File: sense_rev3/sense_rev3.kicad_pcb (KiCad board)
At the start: 2 copper layers, 68 x 52 mm, 46 parts, among them J1 Audio-Jack-4, P1 CONN_02X05, Q1 TSM2301, SW1 SW_SPST, U1 TLV8802, U2 MDBT42Q, U3 PIR, Y1 Crystal

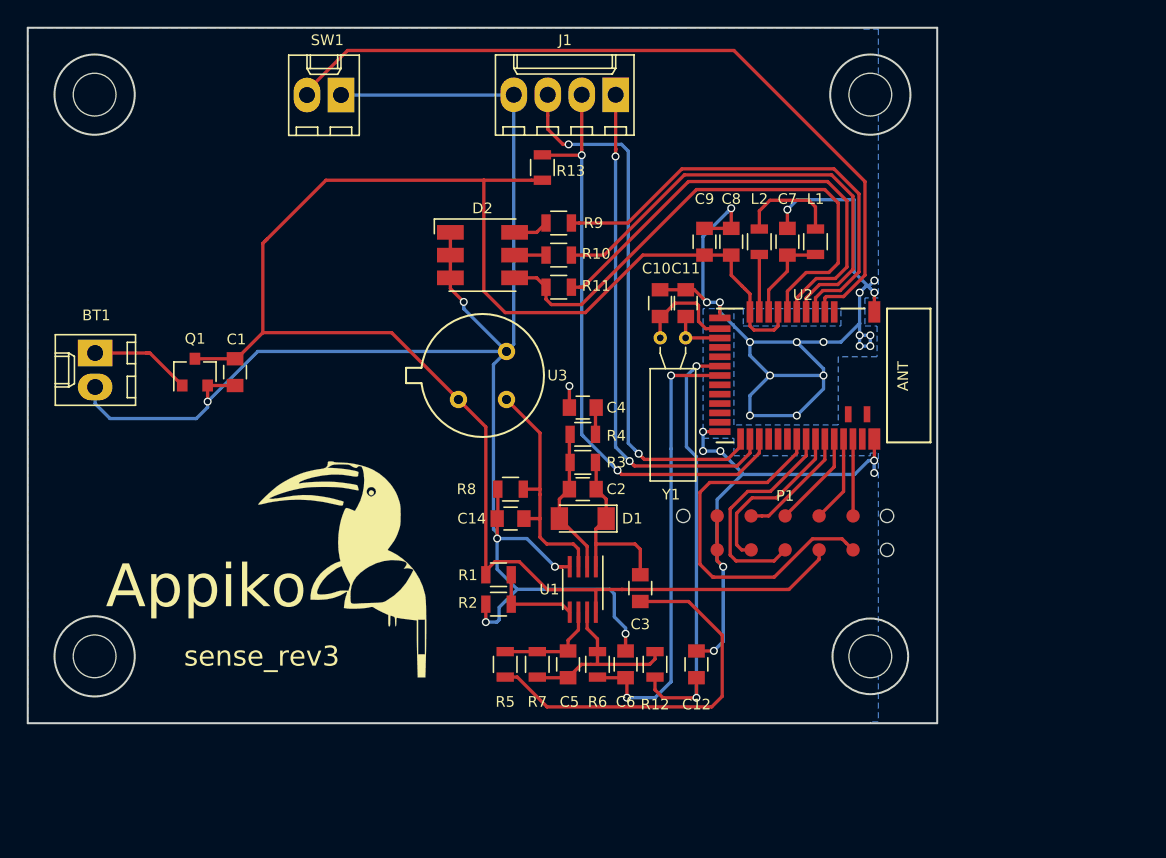
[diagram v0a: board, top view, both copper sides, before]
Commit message: Updated footprints and other files
.pretty files are updated as per the project.
Added images of completed PCBs.
Updated schematics (component names and values).
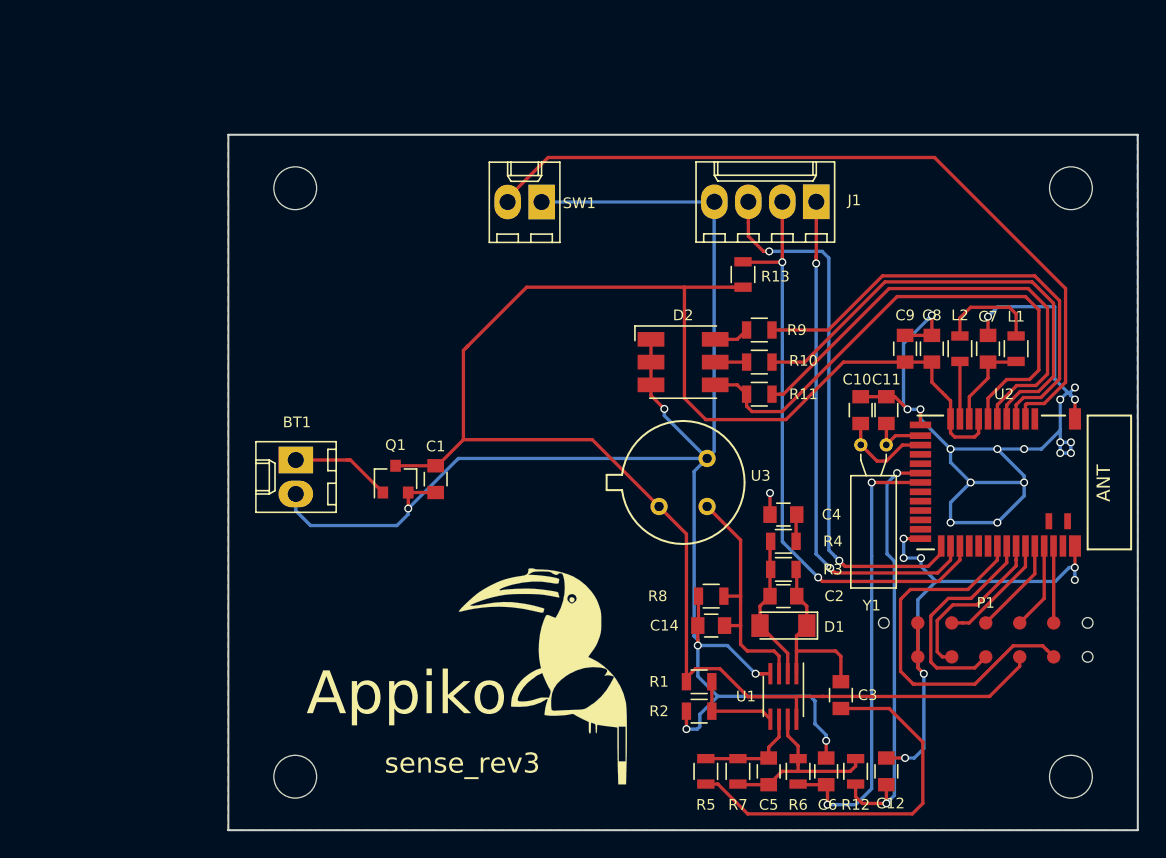
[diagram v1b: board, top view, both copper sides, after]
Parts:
- removed ?: Mounting_Hole1, Mounting_Holes:MountingHole_3.2mm_M3
- removed ?: Mounting_Hole3, Mounting_Holes:MountingHole_3.2mm_M3
- removed ?: Mounting_Hole4, Mounting_Holes:MountingHole_3.2mm_M3
- removed ?: Mounting_Hole2, Mounting_Holes:MountingHole_3.2mm_M3
- added MK1: Mounting_Hole1, sense_rev3_fp:MountingHole_3.2mm_M3, F.Cu at (134.0, 70.0)
- added MK2: Mounting_Hole2, sense_rev3_fp:MountingHole_3.2mm_M3, F.Cu at (192.0, 70.0)
- added MK3: Mounting_Hole3, sense_rev3_fp:MountingHole_3.2mm_M3, F.Cu at (134.0, 114.0)
- added MK4: Mounting_Hole4, sense_rev3_fp:MountingHole_3.2mm_M3, F.Cu at (192.0, 114.0)
- BT1: value 2.6V -> 2 x 1.3V; footprint Connectors_Molex:Molex_KK-6410-02_02x2.54mm_Straight -> sense_rev3_fp:Molex_KK-6410-02_02x2.54mm_Straight
- C1, C10, C11, C12, C14, C2, C3, C4, C5, C6, C7, C8, C9: footprint Capacitors_SMD:C_0805 -> sense_rev3_fp:C_0805
- D1: footprint Diodes_SMD:D_MiniMELF -> sense_rev3_fp:D_MiniMELF
- D2: footprint LEDs:LED_RGB_5050-6 -> sense_rev3_fp:LED_RGB_5050-6
- J1: footprint Connectors_Molex:Molex_KK-6410-04_04x2.54mm_Straight -> sense_rev3_fp:Molex_KK-6410-04_04x2.54mm_Straight
- L1, L2: footprint Inductors_SMD:L_0805 -> sense_rev3_fp:L_0805
- P1: footprint snap_fp:prog_connect -> sense_rev3_fp:prog_connect
- Q1: footprint TO_SOT_Packages_SMD:SOT-23 -> sense_rev3_fp:SOT-23
- R1, R10, R11, R12, R13, R2, R3, R4, R5, R6, R7, R8, R9: footprint Resistors_SMD:R_0805 -> sense_rev3_fp:R_0805
- SW1: footprint Connectors_Molex:Molex_KK-6410-02_02x2.54mm_Straight -> sense_rev3_fp:Molex_KK-6410-02_02x2.54mm_Straight
- U1: footprint Housings_SSOP:SSOP-8_2.95x2.8mm_Pitch0.65mm -> sense_rev3_fp:SSOP-8_2.95x2.8mm_Pitch0.65mm
- U2: footprint detect_trigger:mdbt42Q -> sense_rev3_fp:mdbt42Q
- U3: footprint detect_trigger:PIR_TO5 -> sense_rev3_fp:PIR_TO5
- Y1: footprint Crystals:Crystal_C38-LF_d3.0mm_l8.0mm_Horizontal -> sense_rev3_fp:Crystal_C38-LF_d3.0mm_l8.0mm_Horizontal
- moved J1 17.0 mm to (173.0, 71.0)
- moved C1 17.0 mm to (144.5, 91.8)
- moved C10 17.0 mm to (176.3, 86.6)
- moved C11 17.0 mm to (178.2, 86.6)
- moved C14 17.0 mm to (165.1, 102.7)
- moved C2 17.0 mm to (170.5, 100.5)
- moved C3 17.0 mm to (174.8, 107.9)
- moved C4 17.0 mm to (170.5, 94.4)
- moved C5 17.0 mm to (169.4, 113.6)
- moved C6 17.0 mm to (173.7, 113.6)
- moved C7 17.0 mm to (185.8, 82.0)
- moved C8 17.0 mm to (181.6, 82.0)
- moved C9 17.0 mm to (179.6, 82.0)
- moved D1 17.0 mm to (170.5, 102.7)
- moved D2 17.0 mm to (163.0, 83.0)
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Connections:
- C10 pad 1: /LFCLK_XL1 -> /LFCLK_XL2
- C11 pad 1: /LFCLK_XL2 -> /LFCLK_XL1
- Y1 pad 1: /LFCLK_XL1 -> /LFCLK_XL2
- Y1 pad 2: /LFCLK_XL2 -> /LFCLK_XL1
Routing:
- net /LFCLK_XL1: track 7.98 -> 4.45 mm
- net /LFCLK_XL2: track 4.17 -> 7.06 mm
- net /AMP_OFFSET: track 33.0 -> 32.1 mm
- net GND: track 243.4 -> 244.3 mm
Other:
- outline, holes or cut-outs redrawn
- net class Default: via_dia 0.6 -> 0.5

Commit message: Small changes in PCB
Changed the crystal orientation,
moved reference marking away from vias,
moved the track too close to PIR_OUT in bottom layer.
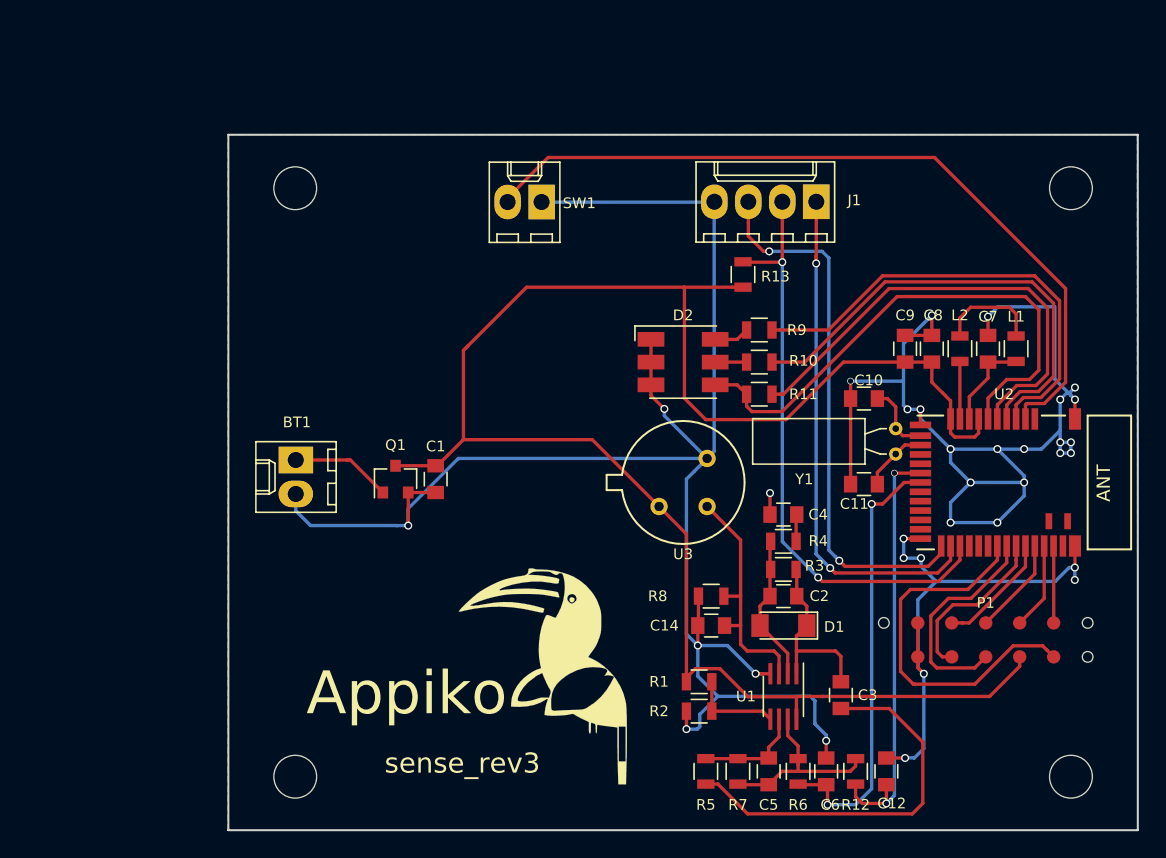
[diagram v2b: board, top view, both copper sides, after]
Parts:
- moved C11 5.78 mm to (176.5, 92.1), turned to 180 degrees
- moved Y1 2.88 mm to (178.9, 88.0), turned to 270 degrees
- moved C10 0.90 mm to (176.5, 85.7), turned to 180 degrees
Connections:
- C10 pad 1: /LFCLK_XL2 -> /LFCLK_XL1
- C11 pad 1: /LFCLK_XL1 -> /LFCLK_XL2
- Y1 pad 1: /LFCLK_XL2 -> /LFCLK_XL1
- Y1 pad 2: /LFCLK_XL1 -> /LFCLK_XL2
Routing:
- net GND: track 244.3 -> 254.3 mm, vias 32 -> 33
- net /LFCLK_XL2: track 7.06 -> 4.95 mm
- net /AMP_SIGNAL: track 33.9 -> 33.0 mm
- net /LFCLK_XL1: track 4.45 -> 5.33 mm
